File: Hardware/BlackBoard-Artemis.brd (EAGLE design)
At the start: 68.6 x 53.3 mm, 87 parts, among them IC3 LM1117, J2 CORTEX_DEBUG, J3 POWER_JACKSUPER_BOMB_DIGITY, J5 USB C, Q1 1.1A/60V/600mΩ, U1 ARTEMIS_FULL, U2 SPH0641LM4H-1, U3 AP2112-3.3V, U4 SPH0641LM4H-1, U5 CH340C, Y1 32.768kHz

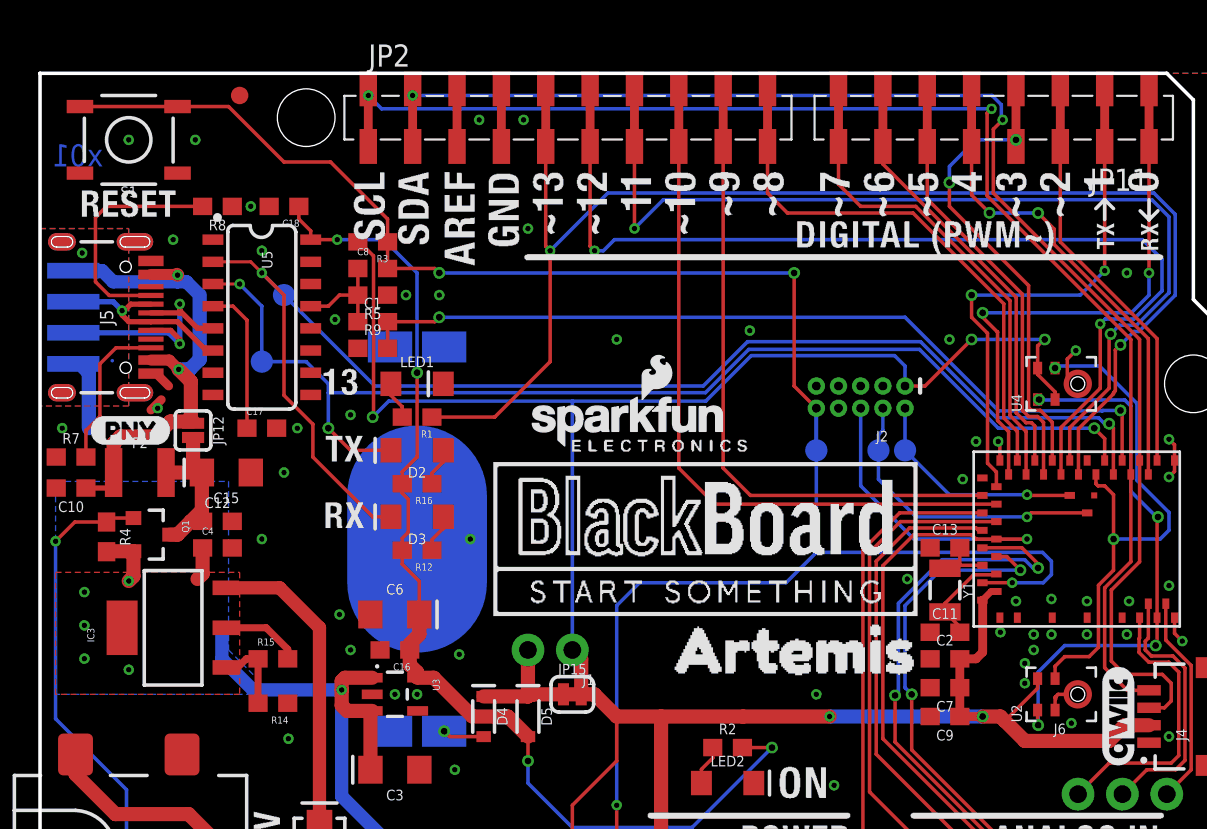
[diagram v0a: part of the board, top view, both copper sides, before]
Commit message: Fix I2C silk. Breakout UART0.
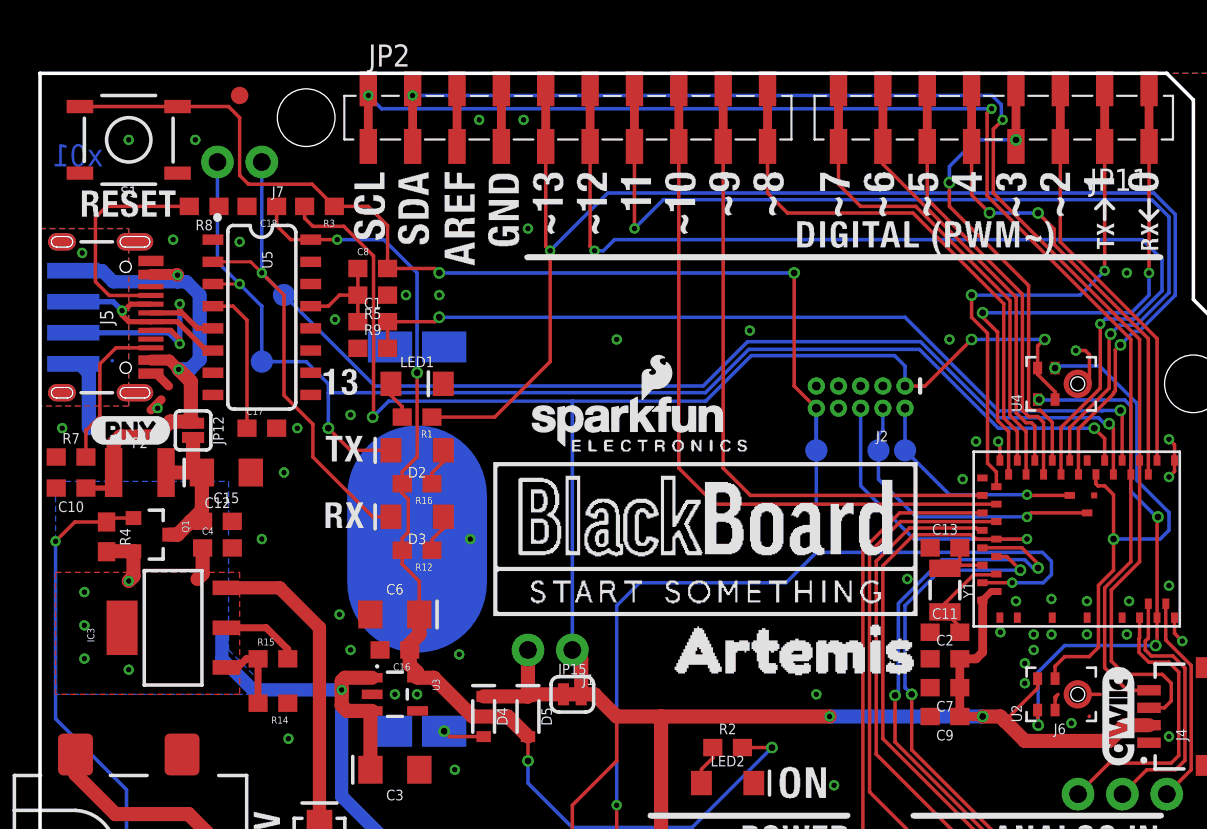
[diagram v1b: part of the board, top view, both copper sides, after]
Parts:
- added J7: (no value), SparkFun-Connectors:1X02_NO_SILK
- added U$18: (no value), buzzard_labels:RX03
- added U$20: (no value), buzzard_labels:TX02
- U1: value ARTEMIS_FULL -> ARTEMIS
- moved R3 3.66 mm to (16.0, 45.7)
- moved C18 1.27 mm to (12.7, 45.7)
- moved R8 0.76 mm to (9.40, 45.7)
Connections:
- net RXI-0: now also J7.1
- net TXO-0: now also J7.2
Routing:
- net TXO-0: track 66.3 -> 73.8 mm
- net RXI-0: track 77.9 -> 84.3 mm
- net VDD: track 156.9 -> 161.1 mm
- net !RESET: track 118.7 -> 120.4 mm
- net 3.3V: track 62.7 -> 63.9 mm
- net CC1: track 13.6 -> 12.8 mm
- net GND: track 19.2 -> 19.8 mm, vias 62 -> 61

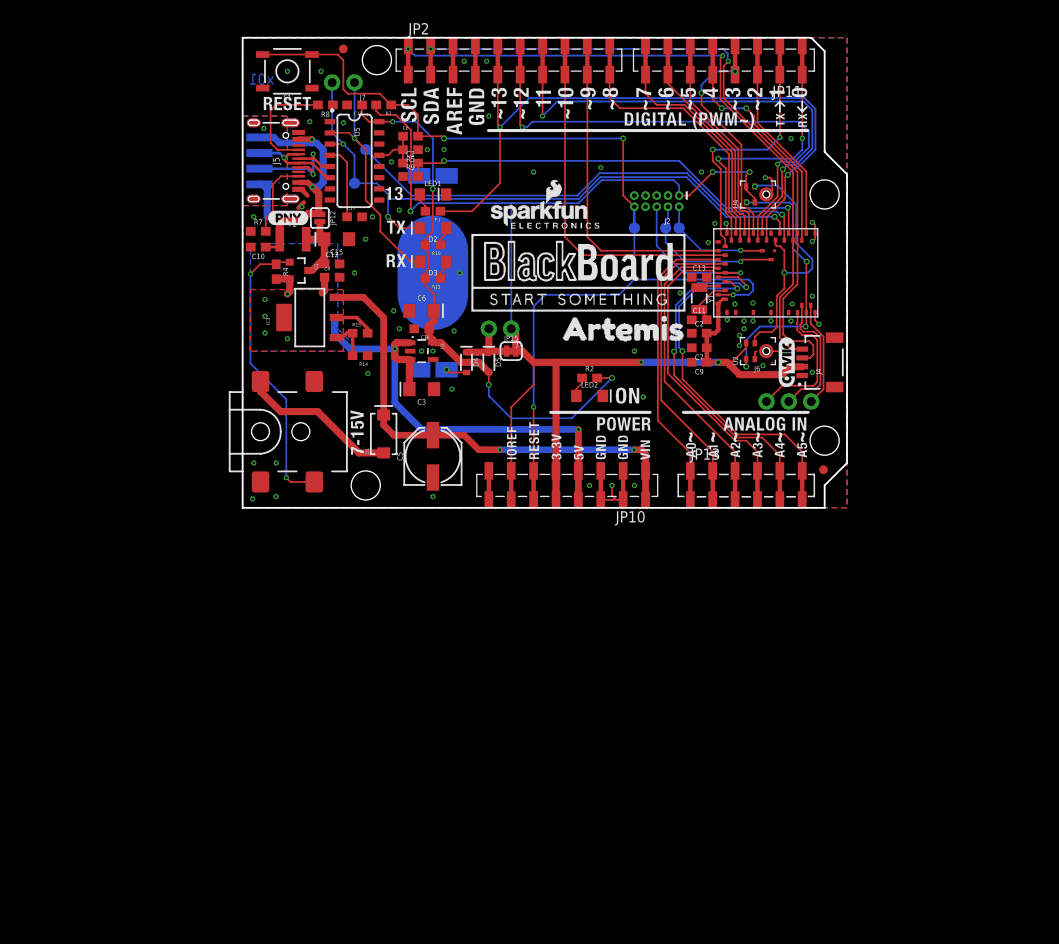
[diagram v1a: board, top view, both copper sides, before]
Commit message: Rev FP for mics. Add decoupling to mics.
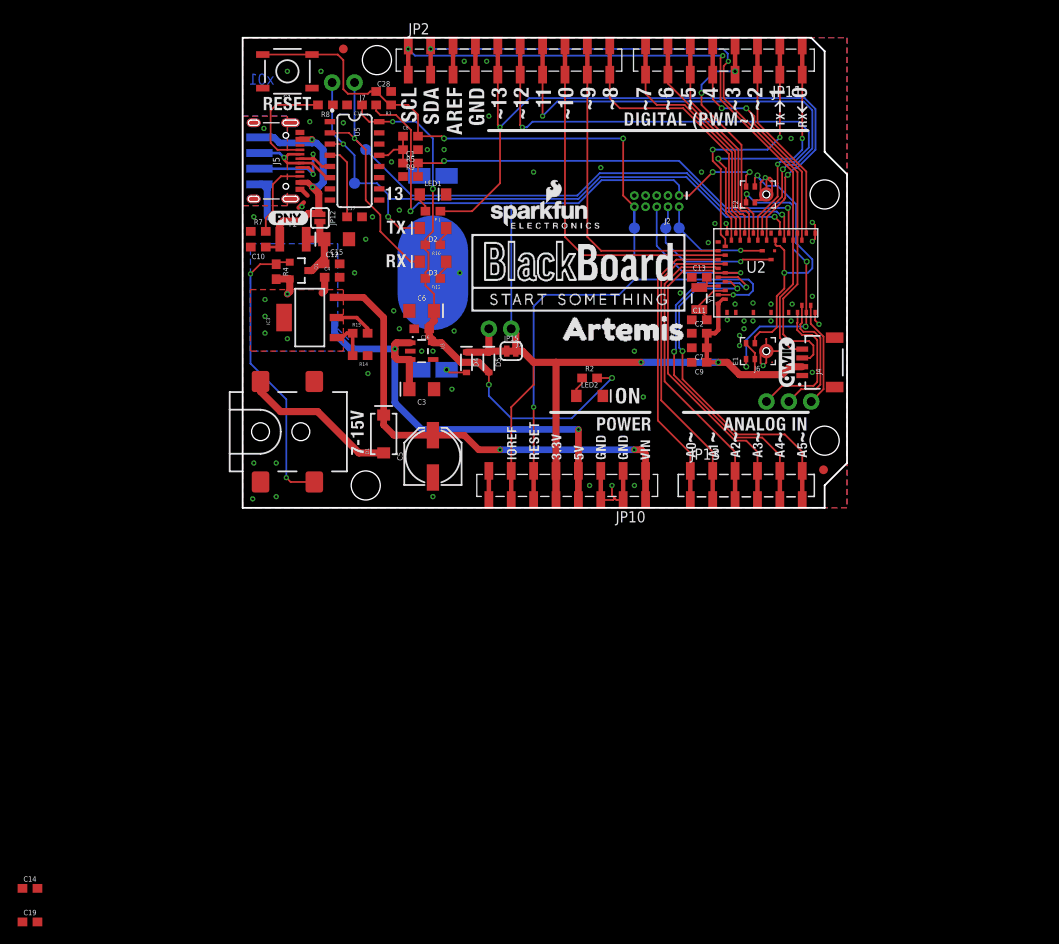
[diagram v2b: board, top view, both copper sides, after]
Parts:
- removed U1: ARTEMIS, Module-Pads:ARTEMIS
- added C14, C19: 0.1uF, SparkFun-Capacitors:0603
- added C28: 1nF, SparkFun-Capacitors:0603
- added E1: SPH0641LM4H-1, SparkFun-Sensors:SPH0641LM4H-1_MICROPHONE
- J5: value USB C -> USB Female Type C Connector
- JP12: value JUMPER-SMT_2_NO_SILK -> (none)
- U2: value SPH0641LM4H-1 -> ARTEMIS_FULL; device SparkFun-Sensors:SPH0641LM4H-1_MICROPHONE -> Module-Pads:ARTEMIS
- moved U2 9.25 mm to (61.0, 26.7), turned to 0 degrees
- renumbered U4 to E2
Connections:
- net !RESET: now also C28.1, U2.33; no longer U1.33
- net BOOT: now also U2.6; no longer U1.6
- net D11/MOSI: now also U2.12; no longer U1.12
- net D4: now also U2.3; no longer U1.3
- net GND: now also C14.2, C19.2, C28.2, E1.3, E1.6, E1.7, E1.8, E2.2, E2.6, E2.7, E2.8, U2.1, U2.20, U2.21, U2.36, U2.37, U2.38, U2.39, U2.40, U2.45; no longer U1.1, U1.20, U1.21, U1.36, U1.37, U1.38, U1.39, U1.40, U1.45, U2.2, U2.3
- net N$7: now also U2.32; no longer U1.32
- net N$8: now also U2.31; no longer U1.31
- net PDMCLK: now also E1.4, U2.9; no longer U1.9, U2.4
- net PDMDATA: now also E1.1, U2.43; no longer U1.43, U2.1
- net RXI-0: now also U2.7; no longer U1.7
- net SDA: now also U2.4; no longer U1.4
- net SWDCK: now also U2.47; no longer U1.47
- net SWDIO: now also U2.46; no longer U1.46
- net TXO-0: now also U2.8; no longer U1.8
- net VDD: now also C14.1, C19.1, E1.2, E1.5, U2.34, U2.35; no longer E2.2, U1.34, U1.35, U2.5
- net ~AD0: now also U2.25; no longer U1.25
- net ~AD1: now also U2.26; no longer U1.26
- net ~AD2: now also U2.27; no longer U1.27
- net ~AD3/SWO: now also U2.28; no longer U1.28
- net ~AD4: now also U2.29; no longer U1.29
- net ~AD5: now also U2.30; no longer U1.30
- net ~D10: now also U2.24; no longer U1.24
- net ~D12/MISO: now also U2.13; no longer U1.13
- net ~D13/SCK: now also U2.11; no longer U1.11
- net ~D14: now also U2.41; no longer U1.41
- net ~D15: now also U2.42; no longer U1.42
- net ~D16: now also U2.44; no longer U1.44
- net ~D2: now also U2.2; no longer U1.2
- net ~D3: now also U2.14; no longer U1.14
- net ~D5: now also U2.15; no longer U1.15
- net ~D6: now also U2.16; no longer U1.16
- net ~D7: now also U2.17; no longer U1.17
- net ~D8: now also U2.18; no longer U1.18
- net ~D9: now also U2.23; no longer U1.23
- net ~RXI-1: now also U2.19; no longer U1.19
- net ~SCL: now also U2.5; no longer U1.5
- net ~TXO-1: now also U2.22; no longer U1.22
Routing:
- net GND: track 19.8 -> 28.9 mm
- net PDMCLK: track 31.6 -> 33.2 mm
- net VDD: track 161.1 -> 159.7 mm
- net PDMDATA: track 31.2 -> 32.5 mm

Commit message: Update power jack. Change to PDM mics.
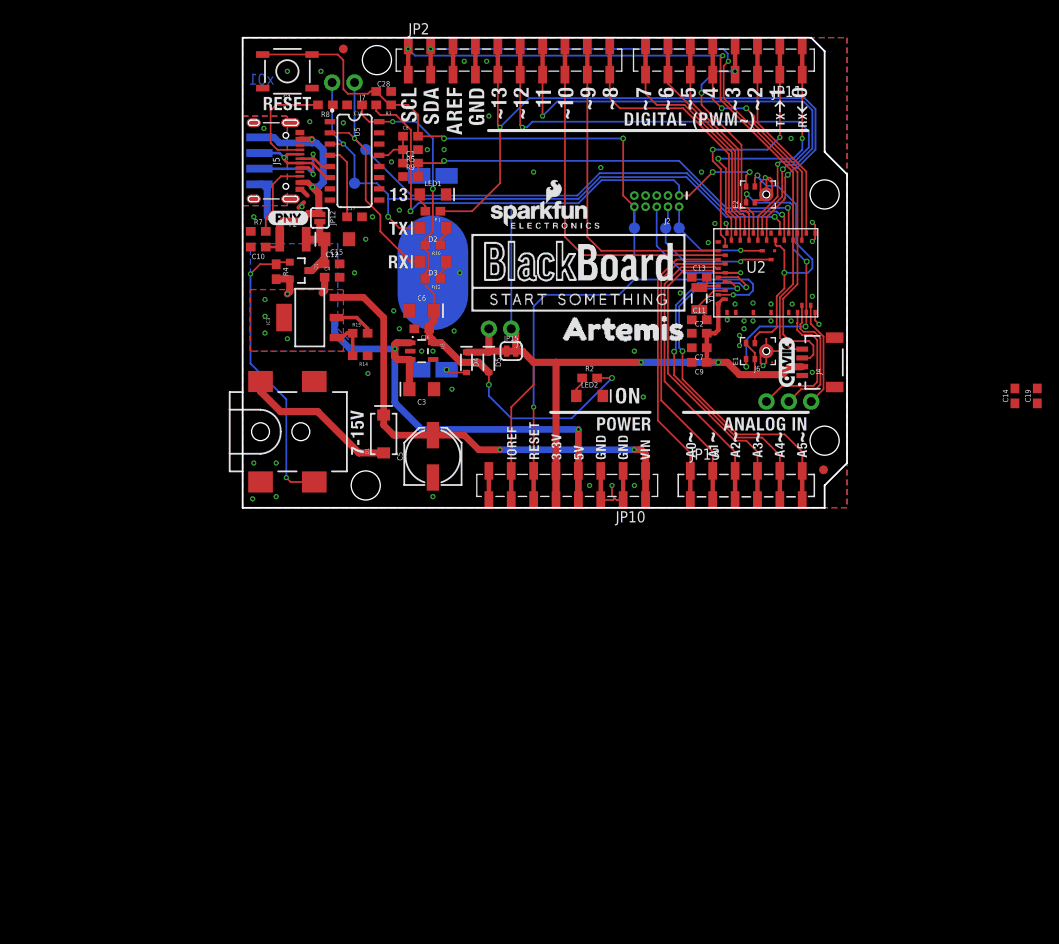
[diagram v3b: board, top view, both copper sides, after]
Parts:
- J3: value POWER_JACKSUPER_BOMB_DIGITY -> POWER_JACKTOE; device Testing:POWER_JACK_SMD_OVERPASTE_SUPER_BOMB_DIGITY -> SparkFun-Connectors:POWER_JACK_SMD_OVERPASTE_TOE
- J5: value USB Female Type C Connector -> USB-C
- LED1: value Blue -> BLUE; device SparkFun-LED:LED-1206-HIDDENSILK -> SparkFun-LED:LED-1206
- moved C19 128.9 mm to (90.2, 12.7), turned to 90 degrees
- moved C14 125.0 mm to (87.6, 12.7), turned to 90 degrees

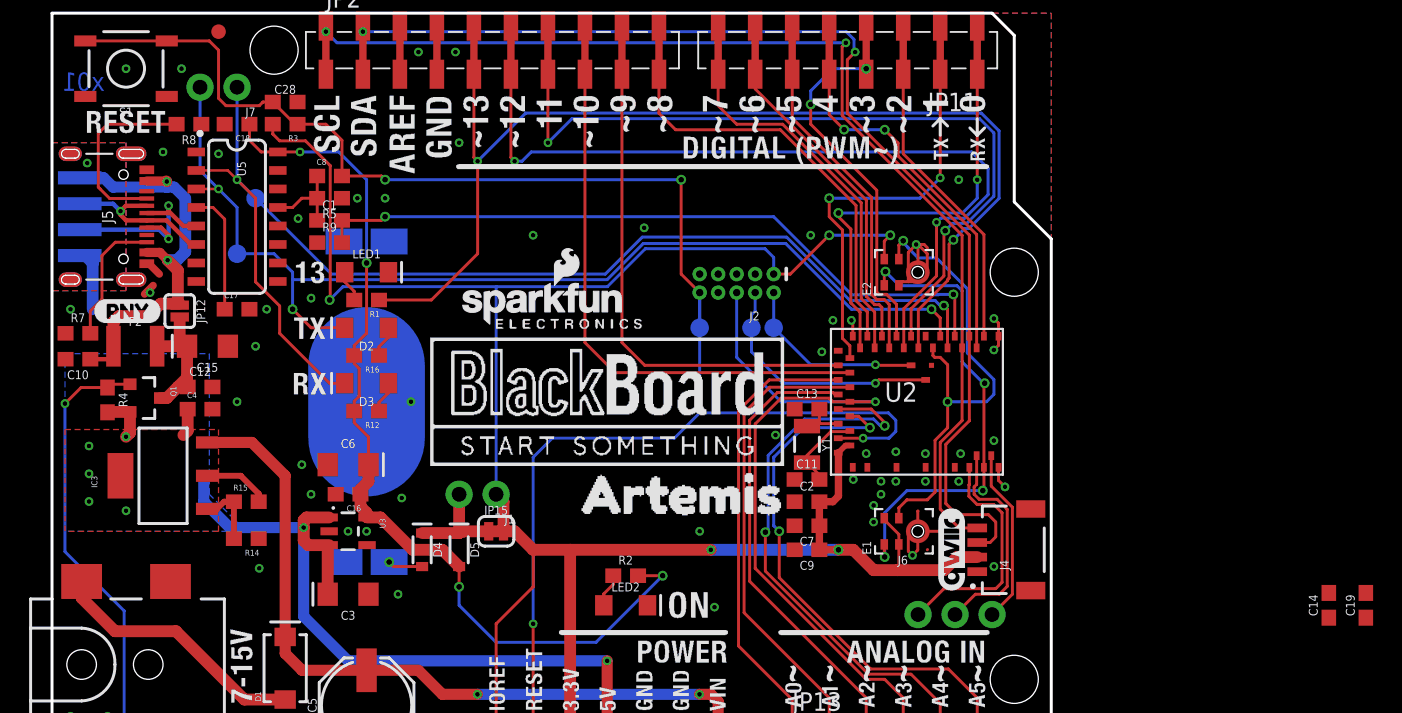
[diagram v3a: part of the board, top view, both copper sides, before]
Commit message: DRC resolved
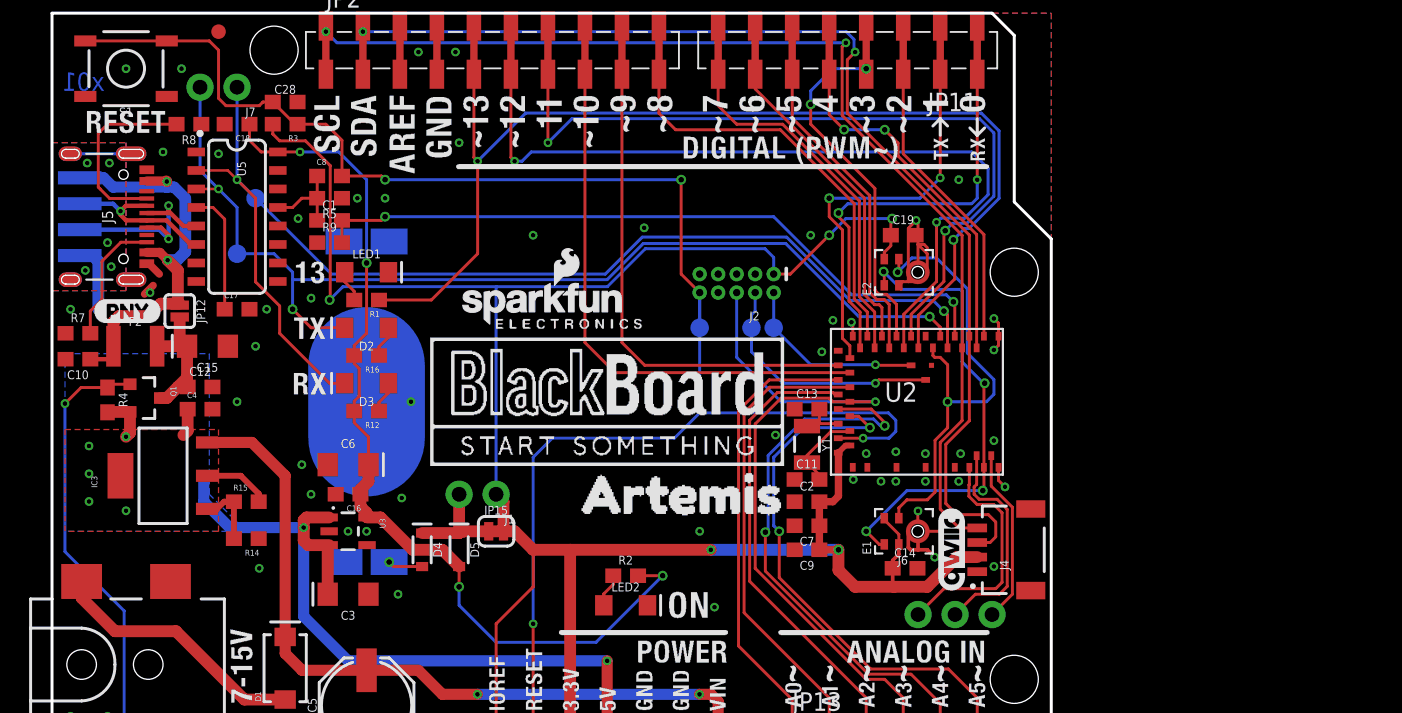
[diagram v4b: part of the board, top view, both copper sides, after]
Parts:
- moved C19 40.7 mm to (58.4, 38.1), turned to 0 degrees
- moved C14 29.2 mm to (58.5, 15.2), turned to 0 degrees
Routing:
- net VDD: track 159.7 -> 164.6 mm
- net GND: track 28.6 -> 33.1 mm, vias 61 -> 59
- net SHLD: track 0.00 -> 4.18 mm, vias 1 -> 5

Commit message: Change 10nF to 0.1uF on auto reset circuit
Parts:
- C8: value 10nF -> 0.1uF
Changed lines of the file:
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@@
 <layer number="47" name="Measures" color="7" fill="1" visible="no" active="yes"/>
 <layer number="48" name="Document" color="7" fill="1" visible="no" active="yes"/>
-<layer number="49" name="ReferenceLC" color="13" fill="1" visible="yes" active="yes"/>
+<layer number="49" name="ReferenceLC" color="13" fill="1" visible="no" active="yes"/>
 <layer number="50" name="ReferenceLS" color="12" fill="1" visible="no" active="yes"/>
 <layer number="51" name="tDocu" color="6" fill="1" visible="yes" active="yes"/>
@@
 <attribute name="VALUE" value="1.1A/60V/600mΩ" x="10.287" y="25.527" size="0.6096" layer="27" ratio="15" rot="R180"/>
 </element>
-<element name="C8" library="SparkFun-Capacitors" package="0603" value="10nF" x="19.05" y="42.164" smashed="yes">
+<element name="C8" library="SparkFun-Capacitors" package="0603" value="0.1uF" x="19.05" y="42.164" smashed="yes">
 <attribute name="NAME" x="18.161" y="42.926" size="0.4064" layer="25" font="vector"/>
-<attribute name="PROD_ID" value="CAP-00867" x="19.05" y="42.164" size="1.778" layer="27" display="off"/>
-<attribute name="VALUE" value="10nF" x="20.574" y="41.91" size="0.6096" layer="27" font="vector" ratio="15"/>
+<attribute name="PROD_ID" value="CAP-00810" x="19.05" y="42.164" size="1.778" layer="27" display="off"/>
+<attribute name="VALUE" value="0.1uF" x="20.574" y="41.91" size="0.6096" layer="27" font="vector" ratio="15"/>
 </element>
 <element name="C10" library="SparkFun-Capacitors" package="0603" value="0.1uF" x="1.778" y="29.591" smashed="yes" rot="R180">
